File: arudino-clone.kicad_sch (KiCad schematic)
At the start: 18 parts

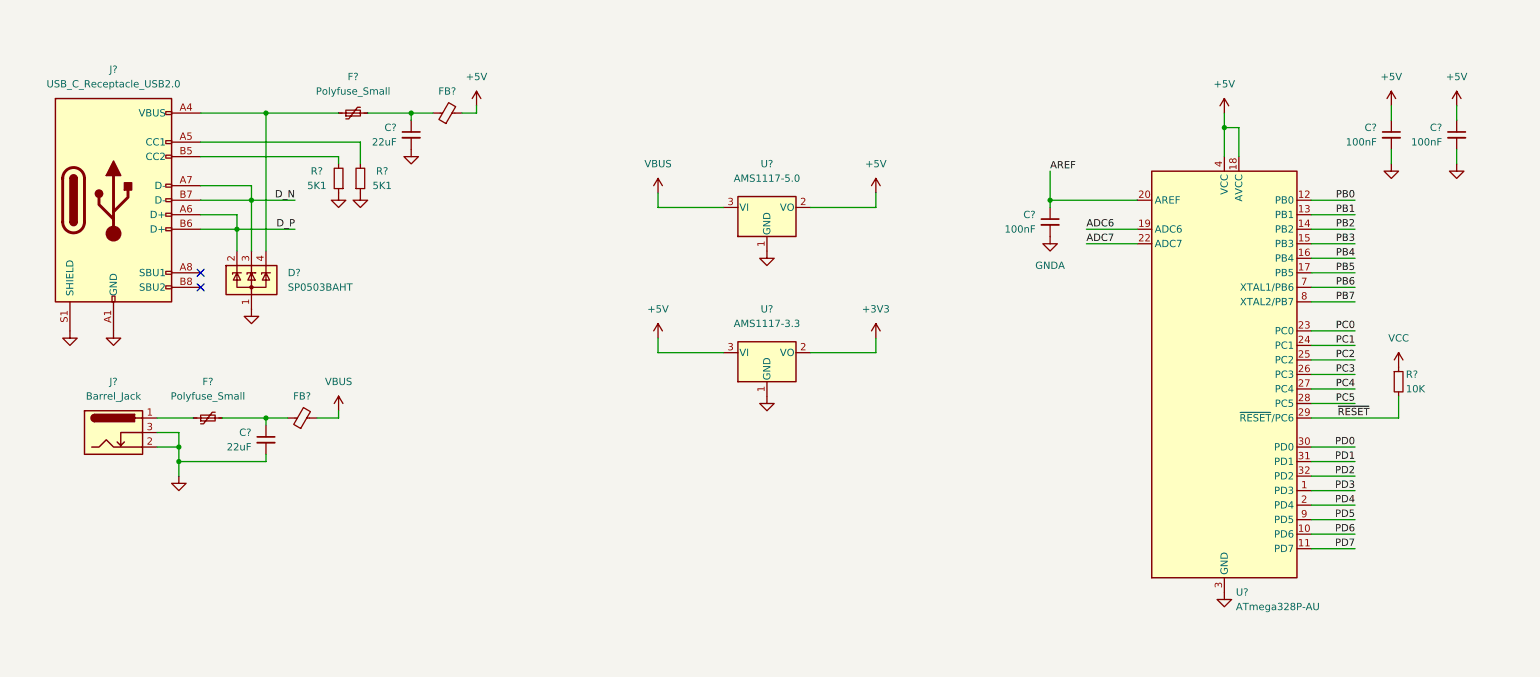
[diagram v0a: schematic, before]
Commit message: add initial components and initial PCB layout
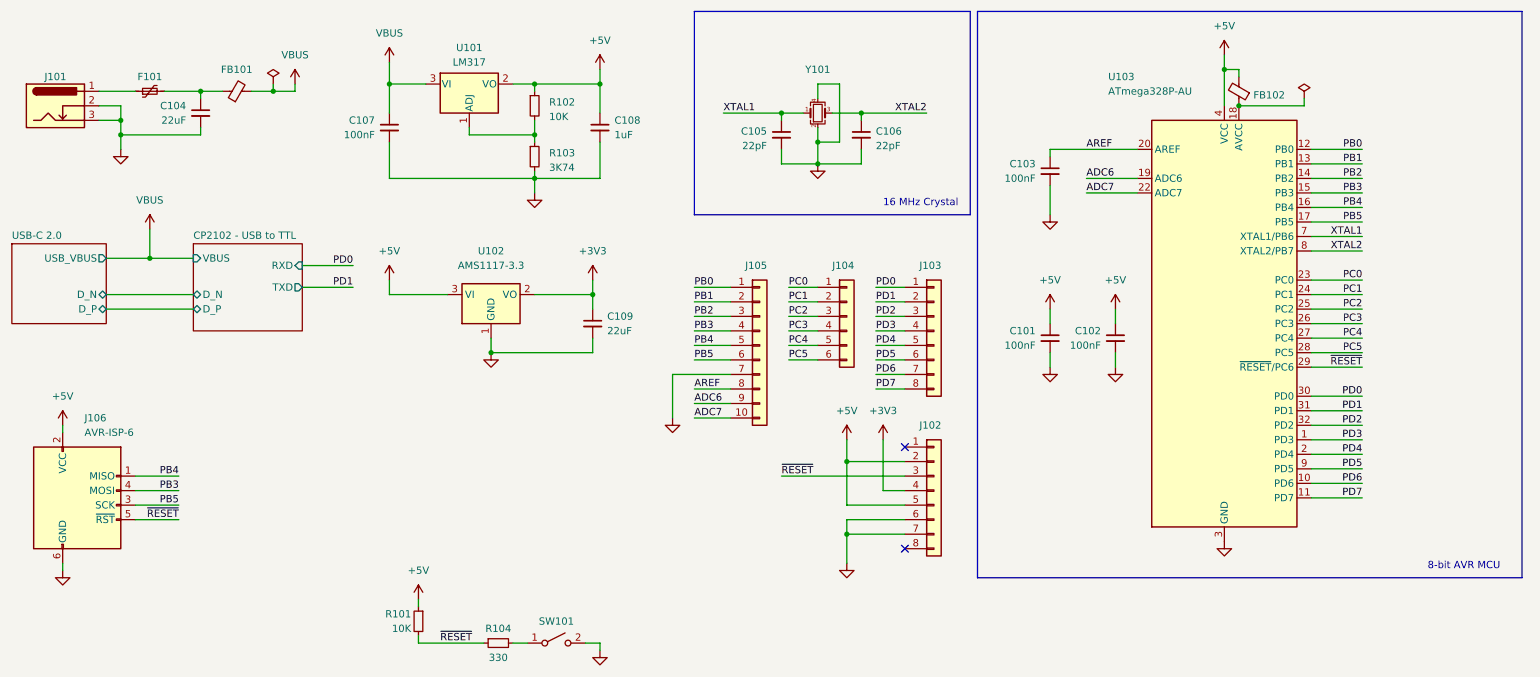
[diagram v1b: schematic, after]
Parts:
- removed C?: 22uF, symbol Device:C_Small
- removed D?: SP0503BAHT, Package_TO_SOT_SMD:SOT-143, symbol Power_Protection:SP0503BAHT
- removed F?: Polyfuse_Small, symbol Device:Polyfuse_Small
- removed FB?: FerriteBead_Small, symbol Device:FerriteBead_Small
- removed J?: USB_C_Receptacle_USB2.0, symbol Connector:USB_C_Receptacle_USB2.0
- removed R? (x2): 5K1, symbol Device:R_Small
- removed U?: AMS1117-5.0, Package_TO_SOT_SMD:SOT-223-3_TabPin2, symbol Regulator_Linear:AMS1117-5.0
- added C105, C106: 22pF, Capacitor_SMD:C_0603_1608Metric, symbol Device:C_Small
- added C107: 100nF, Capacitor_SMD:C_0603_1608Metric, symbol Device:C_Small
- added C108: 1uF, Capacitor_SMD:C_0603_1608Metric, symbol Device:C_Small
- added C109: 22uF, Capacitor_SMD:C_0805_2012Metric, symbol Device:C_Small
- added FB102: FerriteBead_Small, Resistor_SMD:R_0805_2012Metric, symbol Device:FerriteBead_Small
- added J102, J103: Conn_01x08, Connector_PinSocket_2.54mm:PinSocket_1x08_P2.54mm_Vertical, symbol Connector_Generic:Conn_01x08
- added J104: Conn_01x06, Connector_PinSocket_2.54mm:PinSocket_1x06_P2.54mm_Vertical, symbol Connector_Generic:Conn_01x06
- added J105: Conn_01x10, Connector_PinSocket_2.54mm:PinSocket_1x10_P2.54mm_Vertical, symbol Connector_Generic:Conn_01x10
- added J106: AVR-ISP-6, Connector_TAG:TC2030-IDC-NL, symbol Connector:AVR-ISP-6
- added R102: 10K, Resistor_SMD:R_0603_1608Metric, symbol Device:R_Small
- added R103: 3K74, Capacitor_SMD:C_0805_2012Metric, symbol Device:R_Small
- added R104: 330, Resistor_SMD:R_0603_1608Metric, symbol Device:R_Small
- added SW101: SW_SPST, User Custom Footprint:XKB-Connectivity-TS-1187A-B-A-B, symbol Switch:SW_SPST
- added U101: LM317, Package_TO_SOT_SMD:SOT-223-3_TabPin2, symbol Regulator_Linear:LM317_SOT-223
- added Y101: Crystal_GND24_Small, Crystal:Crystal_SMD_3225-4Pin_3.2x2.5mm, symbol Device:Crystal_GND24_Small
- C101, C102, C103: renamed from C?; footprint (none) -> Capacitor_SMD:C_0603_1608Metric; LCSC (none) -> C14663
- C104: renamed from C?; footprint (none) -> Capacitor_SMD:C_0805_2012Metric; LCSC (none) -> C45783
- F101: renamed from F?; footprint (none) -> Fuse:Fuse_1206_3216Metric; LCSC (none) -> C883135
- FB101: renamed from FB?; footprint (none) -> Resistor_SMD:R_0805_2012Metric; LCSC (none) -> C74487
- J101: renamed from J?; symbol Connector:Barrel_Jack_Switch -> Connector:Barrel_Jack_Switch_Pin3Ring; now left out of the parts list
- U102: renamed from U?; LCSC (none) -> C6186
- gave numbers to parts that had none: 2
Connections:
- net GNDA is gone; now on net GND: C103.2
- net VCC is gone; now on net +5V: R101.1
- net +3V3: now also C109.1, J102.4 (Pin_4)
- net +5V: now also C108.1, FB102.2, J102.2 (Pin_2), J102.5 (Pin_5), J106.2 (VCC), R102.1, U101.2 (VO); no longer U103.18 (AVCC)
- net ADC6: now also J105.9 (Pin_9)
- net ADC7: now also J105.10 (Pin_10)
- net AREF: now also J105.8 (Pin_8)
- net GND: now also C105.2, C106.2, C107.2, C108.2, C109.2, J102.6 (Pin_6), J102.7 (Pin_7), J105.7 (Pin_7), J106.6 (GND), R103.2, SW101.2 (B), Y101.2, Y101.4
- net PB0: now also J105.1 (Pin_1)
- net PB1: now also J105.2 (Pin_2)
- net PB2: now also J105.3 (Pin_3)
- net PB3: now also J105.4 (Pin_4), J106.4 (MOSI)
- net PB4: now also J105.5 (Pin_5), J106.1 (MISO)
- net PB5: now also J105.6 (Pin_6), J106.3 (SCK)
- net PC0: now also J104.1 (Pin_1)
- net PC1: now also J104.2 (Pin_2)
- net PC2: now also J104.3 (Pin_3)
- net PC3: now also J104.4 (Pin_4)
- net PC4: now also J104.5 (Pin_5)
- net PC5: now also J104.6 (Pin_6)
- net PD0: now also J103.1 (Pin_1)
- net PD1: now also J103.2 (Pin_2)
- net PD2: now also J103.3 (Pin_3)
- net PD3: now also J103.4 (Pin_4)
- net PD4: now also J103.5 (Pin_5)
- net PD5: now also J103.6 (Pin_6)
- net PD6: now also J103.7 (Pin_7)
- net PD7: now also J103.8 (Pin_8)
- net VBUS: now also C107.1, U101.3 (VI)
- net ~{RESET}: now also J102.3 (Pin_3), J106.5 (~{RST}), R104.1
- net PB6 renamed XTAL1
- net XTAL1: now also C105.1, Y101.1
- net PB7 renamed XTAL2
- net XTAL2: now also C106.1, Y101.3
- new net: R102.2, R103.1, U101.1 (ADJ)
- new net: FB102.1, U103.18 (AVCC)
- new net: R104.2, SW101.1 (A)
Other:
- added sheet CP2102 - USB to TTL (cp2102.kicad_sch)
- added sheet USB-C 2.0 (usbc-2-0.kicad_sch)
- note added: "16 MHz Crystal"
- note added: "8-bit AVR MCU"
- title: (none) -> Arduino Clone (RP2040)
- moved on the sheet: C101, C102, C103, C104, F101, FB101, J101, R101, U102, U103

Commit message: updated caps and power regulator
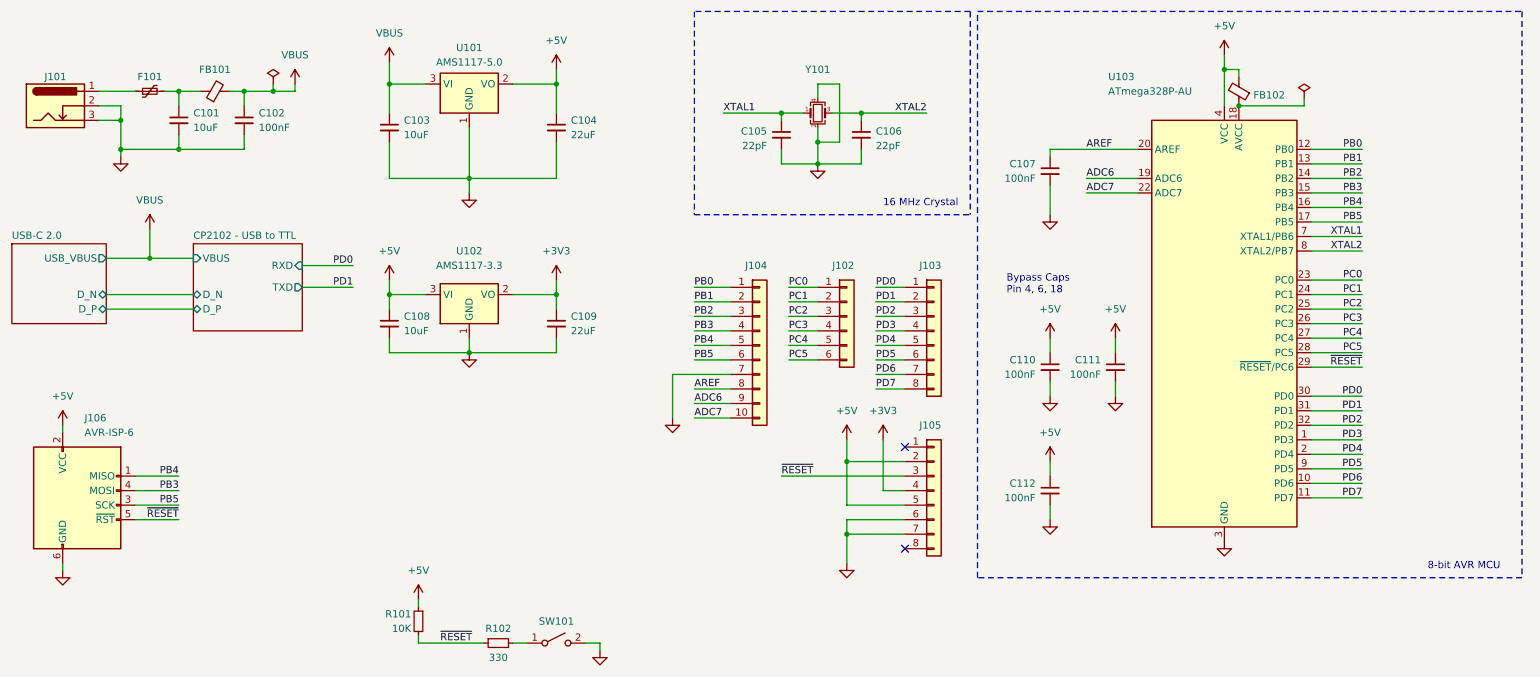
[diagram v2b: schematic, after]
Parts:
- removed C107: 100nF, Capacitor_SMD:C_0603_1608Metric, symbol Device:C_Small
- removed R102: 10K, Resistor_SMD:R_0603_1608Metric, symbol Device:R_Small
- removed R103: 3K74, Capacitor_SMD:C_0805_2012Metric, symbol Device:R_Small
- added C101, C103: 10uF, Capacitor_SMD:C_0805_2012Metric, symbol Device:C_Small
- added C102, C112: 100nF, Capacitor_SMD:C_0603_1608Metric, symbol Device:C_Small
- C108: value 1uF -> 10uF; footprint Capacitor_SMD:C_0603_1608Metric -> Capacitor_SMD:C_0805_2012Metric; LCSC C14663 -> C15850
- U101: value LM317 -> AMS1117-5.0; symbol Regulator_Linear:LM317_SOT-223 -> Regulator_Linear:AMS1117-5.0; LCSC C84244 -> C6187
- renumbered C103 to C107, C101 to C110, C102 to C111, J104 to J102, J105 to J104, J102 to J105, R104 to R102
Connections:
- net +5V: now also C104.1, C112.1
- net GND: now also U101.1 (GND), C101.2, C102.2, C103.2, C112.2
- net VBUS: now also C102.1, C103.1
- net at F101.2, FB101.1: now also C101.1; no longer C104.1
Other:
- note added: "Bypass Caps Pin 4, 6, 18"
- moved on the sheet: C109, C110, C111, FB101, U102
